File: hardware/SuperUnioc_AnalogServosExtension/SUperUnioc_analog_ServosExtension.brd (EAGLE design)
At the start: 100 x 80 mm, 28 parts, among them IC2 74LVC4245APW, IC3 LM2596S-ADJ

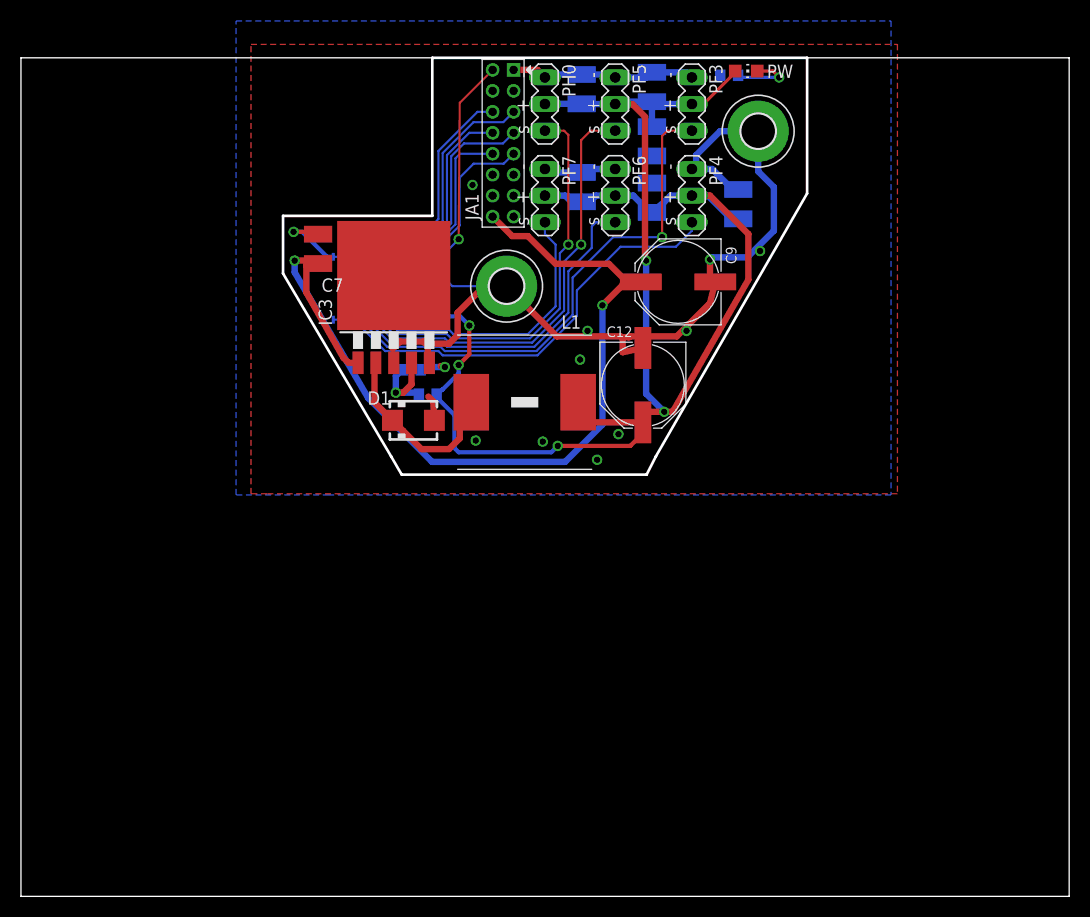
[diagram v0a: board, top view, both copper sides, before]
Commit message: removed dimension rectangle
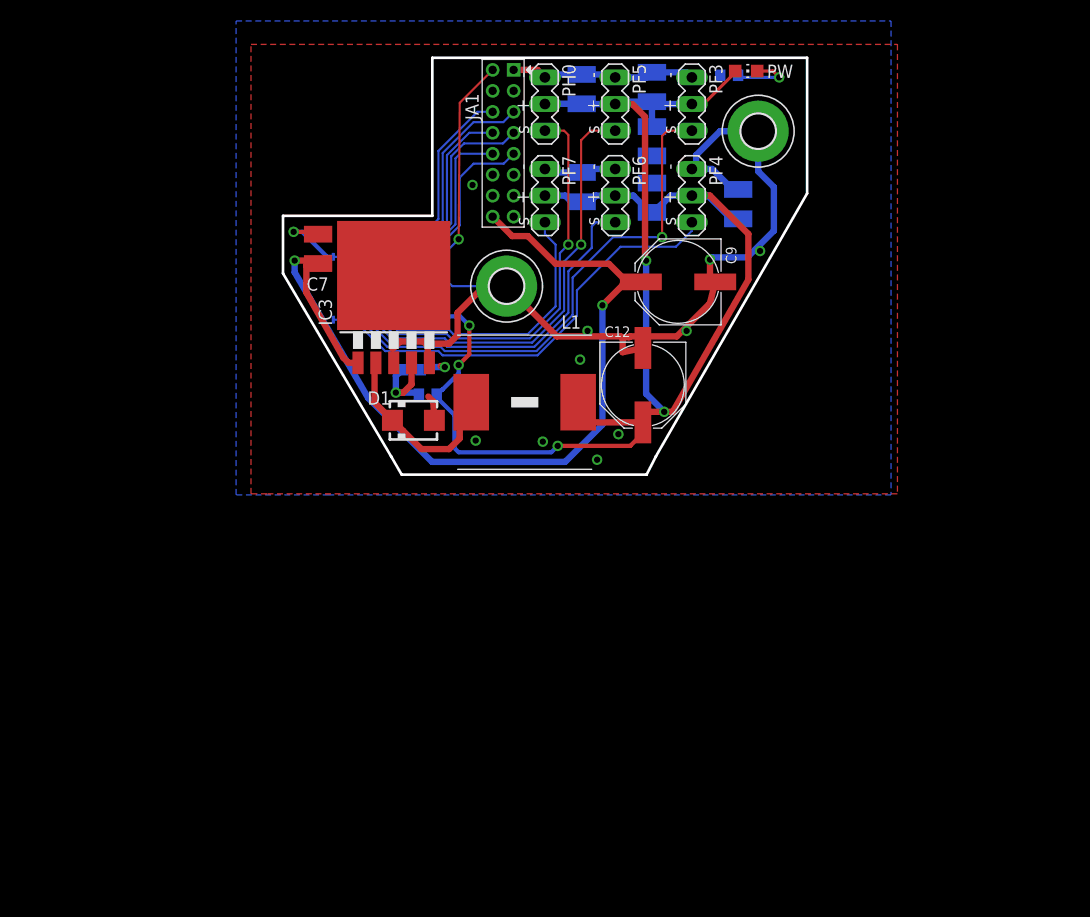
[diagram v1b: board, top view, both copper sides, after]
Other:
- board size 100 x 80 mm -> 50 x 39.8 mm
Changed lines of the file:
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@@
 <grid distance="4" unitdist="mil" unit="mil" style="lines" multiple="1" display="yes" altdistance="0.025" altunitdist="inch" altunit="inch"/>
 <layers>
-<layer number="1" name="Top" color="4" fill="1" visible="yes" active="yes"/>
+<layer number="1" name="Top" color="4" fill="1" visible="no" active="yes"/>
 <layer number="16" name="Bottom" color="1" fill="1" visible="yes" active="yes"/>
 <layer number="17" name="Pads" color="2" fill="1" visible="yes" active="yes"/>
@@
 <layer number="19" name="Unrouted" color="6" fill="1" visible="yes" active="yes"/>
 <layer number="20" name="Dimension" color="15" fill="1" visible="yes" active="yes"/>
-<layer number="21" name="tPlace" color="7" fill="1" visible="yes" active="yes"/>
+<layer number="21" name="tPlace" color="7" fill="1" visible="no" active="yes"/>
 <layer number="22" name="bPlace" color="7" fill="1" visible="yes" active="yes"/>
 <layer number="23" name="tOrigins" color="15" fill="1" visible="yes" active="yes"/>
 <layer number="24" name="bOrigins" color="15" fill="1" visible="yes" active="yes"/>
-<layer number="25" name="tNames" color="7" fill="1" visible="yes" active="yes"/>
+<layer number="25" name="tNames" color="7" fill="1" visible="no" active="yes"/>
 <layer number="26" name="bNames" color="7" fill="1" visible="yes" active="yes"/>
 <layer number="27" name="tValues" color="7" fill="1" visible="no" active="yes"/>
@@
 <board>
 <plain>
-<wire x1="0" y1="0" x2="100" y2="0" width="0" layer="20"/>
-<wire x1="100" y1="0" x2="100" y2="80" width="0" layer="20"/>
-<wire x1="100" y1="80" x2="75" y2="80" width="0" layer="20"/>
-<wire x1="39.243" y1="80" x2="0" y2="80" width="0" layer="20"/>
-<wire x1="0" y1="80" x2="0" y2="0" width="0" layer="20"/>
 <wire x1="5.75" y1="80" x2="39.624" y2="80" width="0.254" layer="49"/>
 <wire x1="74.9808" y1="80" x2="86.75" y2="80" width="0.254" layer="49"/>
@@
 </element>
 <element name="C12" library="robotter_capacitor" package="PANASONIC_F" value="220µF 35V" x="59.3344" y="48.768" smashed="yes" rot="R270">
-<attribute name="NAME" x="55.87" y="53.3628" size="1.016" layer="25"/>
+<attribute name="NAME" x="55.6668" y="53.3628" size="1.016" layer="25"/>
 <attribute name="VALUE" value="220µF 35V" x="56.6594" y="51.318" size="1.016" layer="27" rot="R270"/>
 <attribute name="RS" value="568-828" x="59.3344" y="48.768" size="1.778" layer="27" rot="R270" display="off"/>
@@
 <attribute name="VALUE" x="37.9222" y="48.3362" size="1.27" layer="28" rot="MR0"/>
 </element>
-<element name="R1" library="robotter_resistor" package="R0603" value="3k 1%" x="38.8112" y="47.9044" rot="MR180">
+<element name="R1" library="robotter_resistor" package="R0603" value="3k 1%" x="38.8112" y="47.9044" smashed="yes" rot="MR180">
 <attribute name="RS" value="708-7574" x="38.8112" y="47.9044" size="1.778" layer="28" rot="MR180" display="off"/>
+<attribute name="NAME" x="37.5666" y="47.0662" size="1.27" layer="26" rot="MR180"/>
+<attribute name="VALUE" x="38.1762" y="49.8094" size="1.27" layer="28" rot="MR180"/>
 </element>
 <element name="IC2" library="robotter_ic" package="TSSOP24" value="74LVC4245APW" x="33.3756" y="58.0136" smashed="yes" rot="MR0">
@@
 <attribute name="RS" value="605-8847" x="12.98" y="48.9876" size="1.778" layer="27" rot="R270" display="off"/>
 <attribute name="FARNELL" value="1109794" x="12.98" y="48.9876" size="1.778" layer="27" rot="R270" display="off"/>
-<attribute name="NAME" x="42.396" y="67.046" size="1.27" layer="25" rot="R270"/>
+<attribute name="NAME" x="42.396" y="76.5964" size="1.27" layer="25" rot="R270"/>
 <attribute name="VALUE" x="42" y="79.8476" size="1.27" layer="27" rot="R270"/>
 </element>
@@
 <element name="C7" library="robotter_capacitor" package="C1210" value="10µF 25V" x="28.3464" y="61.7728" smashed="yes" rot="R90">
 <attribute name="RS" value="766-1185 " x="28.3464" y="61.7728" size="1.778" layer="27" rot="R90" display="off"/>
-<attribute name="NAME" x="28.6766" y="57.6834" size="1.27" layer="25"/>
+<attribute name="NAME" x="27.2542" y="57.785" size="1.27" layer="25"/>
 <attribute name="VALUE" x="31.5214" y="59.8678" size="1.27" layer="27" rot="R90"/>
 </element>
